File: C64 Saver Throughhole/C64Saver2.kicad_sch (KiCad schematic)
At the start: 24 parts, among them J1 Conn_01x04, J2 Conn_01x08, J4 Conn_01x08, J5 Conn_01x04, J6 Conn_01x04, Q1 BC547, Q2 IRFR5305, U1 TL431LP

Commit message: 2.7 with iBom and gerbers
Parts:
- added R2: 330 1%, Resistor_THT:R_Axial_DIN0204_L3.6mm_D1.6mm_P5.08mm_Horizontal, symbol C64Saver2-rescue:R
- LED1: footprint LED_THT:LED_D3.0mm -> LED_THT:LED_D3.0mm_Easy_1
- LED2: footprint LED_THT:LED_D3.0mm -> LED_THT:LED_D3.0mm_Easy_2
- Q1, U1: footprint Package_TO_SOT_THT:TO-92_Inline -> Package_TO_SOT_THT:TO-92_Inline_Wide
- Q2: value IRFR5305 -> IPD068P03L3G
- R10: value 1k -> 330
- R3: renamed from R1; value 3k9 1% -> 3k3 1%
- renumbered R2 to R1, R7 to R11, R5 to R4, R9 to R5, R3 to R6, R8 to R7, R4 to R8, R6 to R9
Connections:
- net 5V_SAFE: now also LED2.2 (A)
- net GND: now also R10.2
- net OVERVOLTAGE: no longer R10.2
- net SENSE: now also R2.2; no longer R3.2
- net VCC1-: no longer LED2.2 (A)
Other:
- note removed: "2.4"

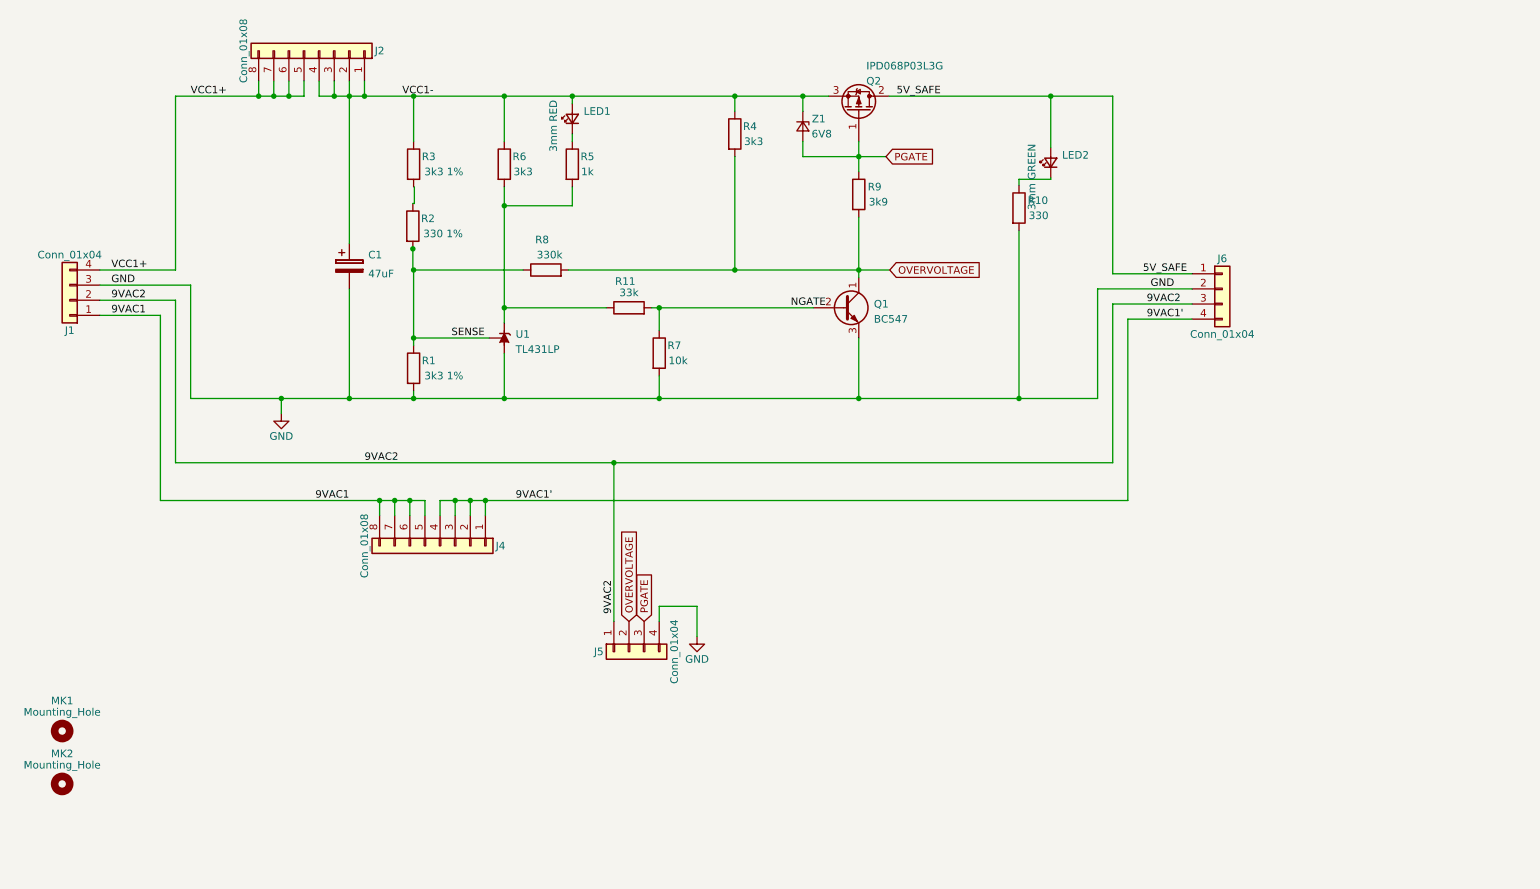
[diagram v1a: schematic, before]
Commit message: Updates to both kicad and easyeda versions. I found a missing connection in the earlier untested Kicad version. :(
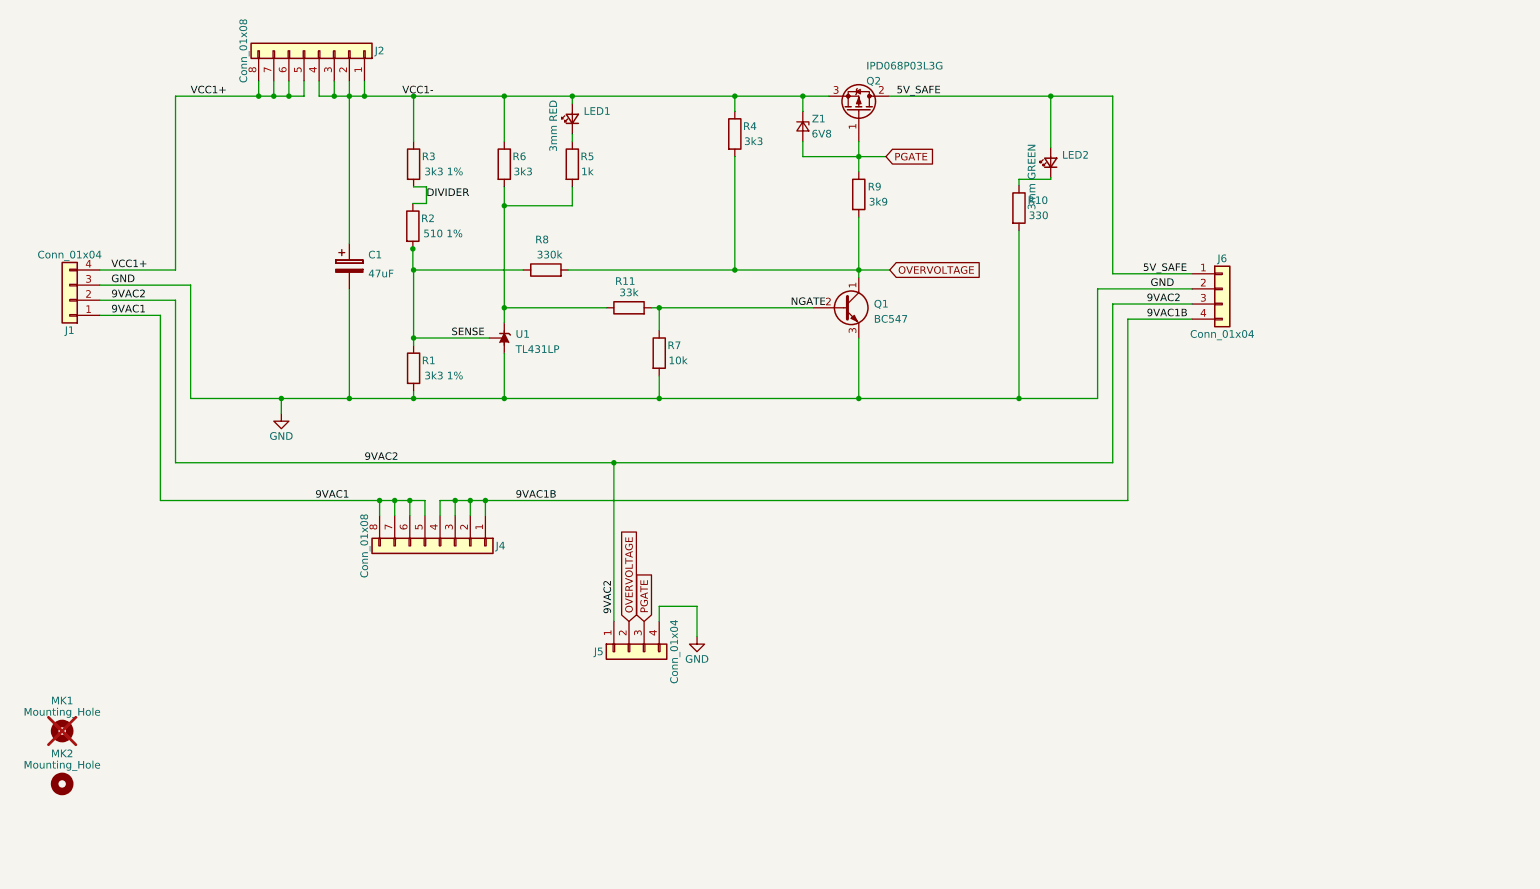
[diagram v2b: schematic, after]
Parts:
- MK1: now not fitted
- R2: value 330 1% -> 510 1%
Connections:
- net DIVIDER: now reaches R3.2
- net DIVIDER: now also R2.1
- net 9VAC1' renamed 9VAC1B
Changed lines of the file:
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@@
   (title_block
     (title "C64 Saver2 THT")
-    (date "2023-10-20")
+    (date "2023-11-18")
     (rev "2.7")
   )
@@
     (stroke (width 0) (type default))
   )
+  (wire (pts (xy 89.154 78.74) (xy 86.995 78.74))
+    (stroke (width 0) (type default))
+  )
   (wire (pts (xy 194.056 77.216) (xy 194.056 77.47))
     (stroke (width 0) (type default))
@@
     (stroke (width 0) (type default))
   )
-  (wire (pts (xy 87.122 78.74) (xy 87.122 81.534))
+  (wire (pts (xy 89.154 78.74) (xy 89.154 81.534))
     (stroke (width 0) (type default))
   )
@@
     (stroke (width 0) (type default))
   )
-  (wire (pts (xy 87.122 81.534) (xy 86.868 81.534))
+  (wire (pts (xy 89.154 81.534) (xy 86.868 81.534))
     (stroke (width 0) (type default))
   )
@@
     (effects (font (size 1.27 1.27)) (justify left bottom))
   )
-  (label "9VAC1'" (at 104.14 131.445 0) (fields_autoplaced)
+  (label "9VAC1B" (at 104.14 131.445 0) (fields_autoplaced)
     (effects (font (size 1.2446 1.2446)) (justify left bottom))
   )
-  (label "9VAC1'" (at 210.185 100.965 0) (fields_autoplaced)
+  (label "9VAC1B" (at 210.185 100.965 0) (fields_autoplaced)
     (effects (font (size 1.2446 1.2446)) (justify left bottom))
   )
@@
   (label "9VAC2" (at 78.74 125.095 0) (fields_autoplaced)
     (effects (font (size 1.2446 1.2446)) (justify left bottom))
+  )
+  (label "DIVIDER" (at 89.154 80.772 0) (fields_autoplaced)
+    (effects (font (size 1.27 1.27)) (justify left bottom))
   )
   (label "5V_SAFE" (at 209.55 93.345 0) (fields_autoplaced)
@@
   )
   (symbol (lib_id "C64Saver2-rescue:Mounting_Hole") (at 27.94 170.18 0) (unit 1)
-    (in_bom no) (on_board yes) (dnp no)
+    (in_bom no) (on_board yes) (dnp yes)
     (property "Reference" "MK1" (at 27.94 165.1 0)
       (effects (font (size 1.27 1.27)))
@@
     )
     (property "kessler" "-" (at 27.94 170.18 0)
+      (effects (font (size 1.27 1.27)) hide)
+    )
+    (property "Sim.Enable" "0" (at 27.94 170.18 0)
       (effects (font (size 1.27 1.27)) hide)
     )
@@
       (effects (font (size 1.27 1.27)))
     )
-    (property "Value" "330 1%" (at 91.948 86.614 0)
-      (effects (font (size 1.27 1.27)))
-    )
+    (property "Value" "510 1%" (at 91.948 86.614 0)
+      (effects (font (size 1.27 1.27)))
+    )
